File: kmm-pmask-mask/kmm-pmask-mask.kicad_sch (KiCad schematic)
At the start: 68 parts, among them J1 F31L-1A7H1-11030, U1 MS5611-01BA, U10 MAX30101EFD_T, U11 SHT40-AD1B-R3, U12 SHT40-AD1B-R3, U13 TMP117MAIDRVR, U14 TMP117MAIDRVR, U15 TCA9546APW, U2 MAX30101EFD_T, U3 SHT40-AD1B-R3, U4 TMP117MAIDRVR, U5 MS5611-01BA, U6 MS5611-01BA, U7 MS5611-01BA, U8 MAX30101EFD_T, U9 MAX30101EFD_T

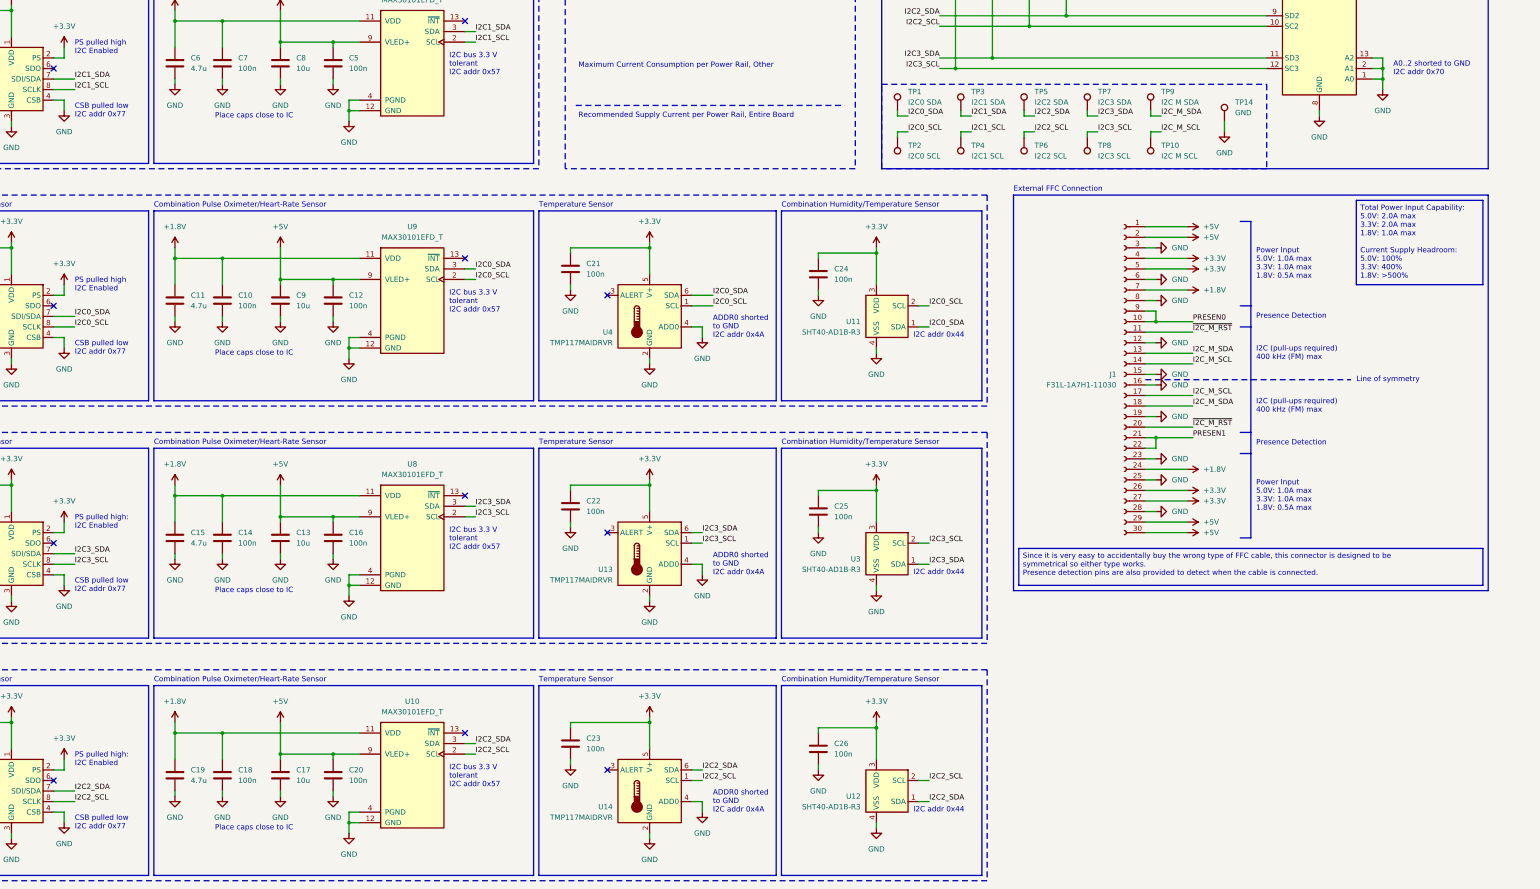
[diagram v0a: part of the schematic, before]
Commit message: Add annotations of bus load
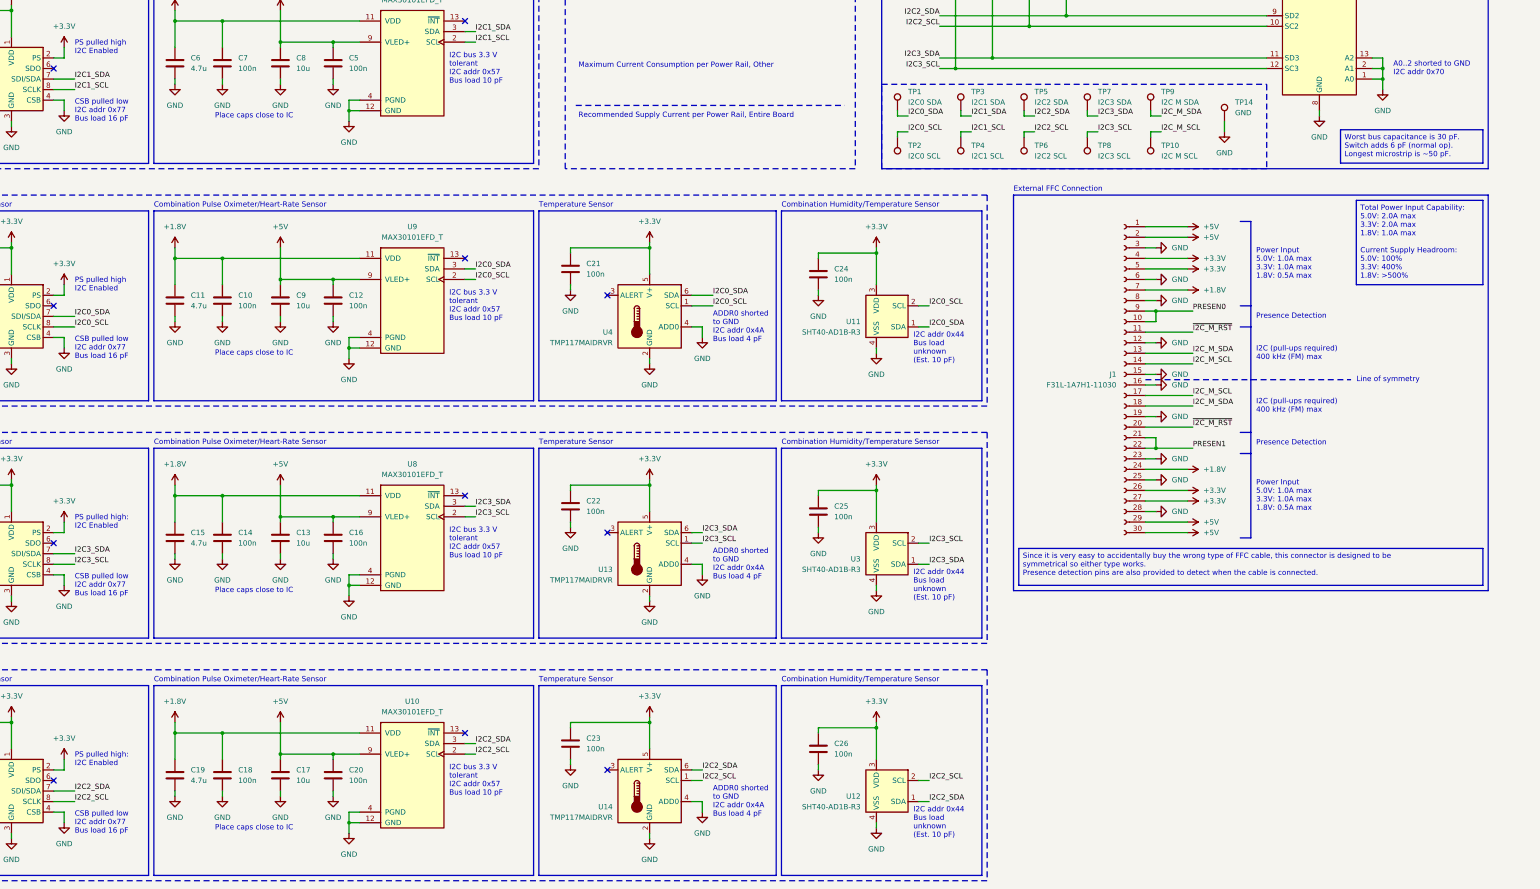
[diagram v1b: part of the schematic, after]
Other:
- note added: "ADDR0 shorted to GND I2C addr 0x4A Bus load 4 pF"
- note added: "CSB pulled low I2C addr 0x77 Bus load 16 pF"
- note added: "I2C addr 0x44 Bus load unknown (Est. 10 pF)"
- note added: "I2C bus 3.3 V tolerant I2C addr 0x57 Bus load 10 pF"
- note removed: "ADDR0 shorted to GND I2C addr 0x4A"
- note removed: "CSB pulled low I2C addr 0x77"
- note removed: "I2C addr 0x44"
- note removed: "I2C bus 3.3 V tolerant I2C addr 0x57"
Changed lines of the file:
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@@
 		)
 	)
-	(text "CSB pulled low\nI2C addr 0x77"
+	(text "CSB pulled low\nI2C addr 0x77\nBus load 16 pF"
 		(exclude_from_sim no)
 		(at 59.69 208.28 0)
@@
 		)
 	)
-	(text "ADDR0 shorted\nto GND\nI2C addr 0x4A"
+	(text "ADDR0 shorted\nto GND\nI2C addr 0x4A\nBus load 4 pF"
 		(exclude_from_sim no)
 		(at 213.36 260.35 0)
@@
 		)
 	)
-	(text "I2C bus 3.3 V\ntolerant\nI2C addr 0x57"
+	(text "I2C bus 3.3 V\ntolerant\nI2C addr 0x57\nBus load 10 pF"
 		(exclude_from_sim no)
 		(at 149.86 80.01 0)
@@
 		)
 	)
-	(text "CSB pulled low\nI2C addr 0x77"
+	(text "CSB pulled low\nI2C addr 0x77\nBus load 16 pF"
 		(exclude_from_sim no)
 		(at 59.69 151.13 0)
@@
 		)
 	)
-	(text "ADDR0 shorted\nto GND\nI2C addr 0x4A"
+	(text "ADDR0 shorted\nto GND\nI2C addr 0x4A\nBus load 4 pF"
 		(exclude_from_sim no)
 		(at 213.36 146.05 0)
@@
 		)
 	)
-	(text "I2C bus 3.3 V\ntolerant\nI2C addr 0x57"
+	(text "I2C bus 3.3 V\ntolerant\nI2C addr 0x57\nBus load 10 pF"
 		(exclude_from_sim no)
 		(at 149.86 194.31 0)
@@
 		)
 	)
-	(text "I2C addr 0x44"
+	(text "I2C addr 0x44\nBus load\nunknown\n(Est. 10 pF)"
 		(exclude_from_sim no)
 		(at 261.62 147.32 0)
@@
 		)
 	)
-	(text "CSB pulled low\nI2C addr 0x77"
+	(text "CSB pulled low\nI2C addr 0x77\nBus load 16 pF"
 		(exclude_from_sim no)
 		(at 59.69 93.98 0)
@@
 		)
 	)
-	(text "ADDR0 shorted\nto GND\nI2C addr 0x4A"
+	(text "ADDR0 shorted\nto GND\nI2C addr 0x4A\nBus load 4 pF"
 		(exclude_from_sim no)
 		(at 213.36 203.2 0)
@@
 		)
 	)
-	(text "I2C bus 3.3 V\ntolerant\nI2C addr 0x57"
+	(text "I2C bus 3.3 V\ntolerant\nI2C addr 0x57\nBus load 10 pF"
 		(exclude_from_sim no)
 		(at 149.86 251.46 0)
@@
 		)
 	)
-	(text "I2C addr 0x44"
+	(text "I2C addr 0x44\nBus load\nunknown\n(Est. 10 pF)"
 		(exclude_from_sim no)
 		(at 261.62 261.62 0)
@@
 		)
 	)
-	(text "I2C bus 3.3 V\ntolerant\nI2C addr 0x57"
+	(text "I2C bus 3.3 V\ntolerant\nI2C addr 0x57\nBus load 10 pF"
 		(exclude_from_sim no)
 		(at 149.86 137.16 0)
@@
 		)
 	)
-	(text "CSB pulled low\nI2C addr 0x77"
+	(text "CSB pulled low\nI2C addr 0x77\nBus load 16 pF"
 		(exclude_from_sim no)
 		(at 59.69 265.43 0)
@@
 		)
 	)
-	(text "I2C addr 0x44"
+	(text "I2C addr 0x44\nBus load\nunknown\n(Est. 10 pF)"
 		(exclude_from_sim no)
 		(at 261.62 204.47 0)
@@
 		)
 	)
+	(text_box "Worst bus capacitance is 30 pF.\nSwitch adds 6 pF (normal op).\nLongest microstrip is ~50 pF."
+		(exclude_from_sim no)
+		(at 364.49 98.5646 0)
+		(size 34.29 8.0376)
+		(margins 0.9525 0.9525 0.9525 0.9525)
+		(stroke
+			(width 0)
+			(type solid)
+		)
+		(fill
+			(type none)
+		)
+		(effects
+			(font
+				(size 1.27 1.27)
+			)
+			(justify left top)
+		)
+	)
 	(junction
 		(at 298.45 71.12)
@@
 	)
 	(junction
-		(at 125.73 265.43)
+		(at 320.04 175.26)
 		(diameter 0)
 		(color 0 0 0 0)
 	)
 	(junction
-		(at 109.22 134.62)
+		(at 125.73 265.43)
 		(diameter 0)
 		(color 0 0 0 0)
 	)
 	(junction
-		(at 95.25 72.39)
+		(at 109.22 134.62)
 		(diameter 0)
 		(color 0 0 0 0)
 	)
 	(junction
-		(at 320.04 144.78)
+		(at 95.25 72.39)
 		(diameter 0)
 		(color 0 0 0 0)
@@
 	)
 	(junction
+		(at 320.04 142.24)
+		(diameter 0)
+		(color 0 0 0 0)
+	)
+	(junction
 		(at 198.12 127)
 		(diameter 0)
@@
 	)
 	(junction
-		(at 320.04 172.72)
-		(diameter 0)
-		(color 0 0 0 0)
-	)
-	(junction
 		(at 83.82 129.54)
 		(diameter 0)
@@
 	(wire
 		(pts
-			(xy 320.04 172.72) (xy 320.04 175.26)
-		)
-		(stroke
-			(width 0)
-			(type default)
-		)
-	)
-	(wire
-		(pts
 			(xy 95.25 243.84) (xy 128.27 243.84)
 		)
@@
 	(wire
 		(pts
-			(xy 320.04 172.72) (xy 328.93 172.72)
+			(xy 320.04 175.26) (xy 328.93 175.26)
 		)
 		(stroke
@@
 	(wire
 		(pts
-			(xy 320.04 144.78) (xy 328.93 144.78)
+			(xy 320.04 142.24) (xy 328.93 142.24)
 		)
 		(stroke
@@
 		)
 	)
+	(wire
+		(pts
+			(xy 320.04 175.26) (xy 320.04 172.72)
+		)
+		(stroke
+			(width 0)
+			(type default)
+		)
+	)
 	(polyline
 		(pts
@@
 	)
 	(label "PRESEN1"
-		(at 328.93 172.72 0)
+		(at 328.93 175.26 0)
 		(effects
 			(font
@@
 	)
 	(label "PRESEN0"
-		(at 328.93 144.78 0)
+		(at 328.93 142.24 0)
 		(effects
 			(font

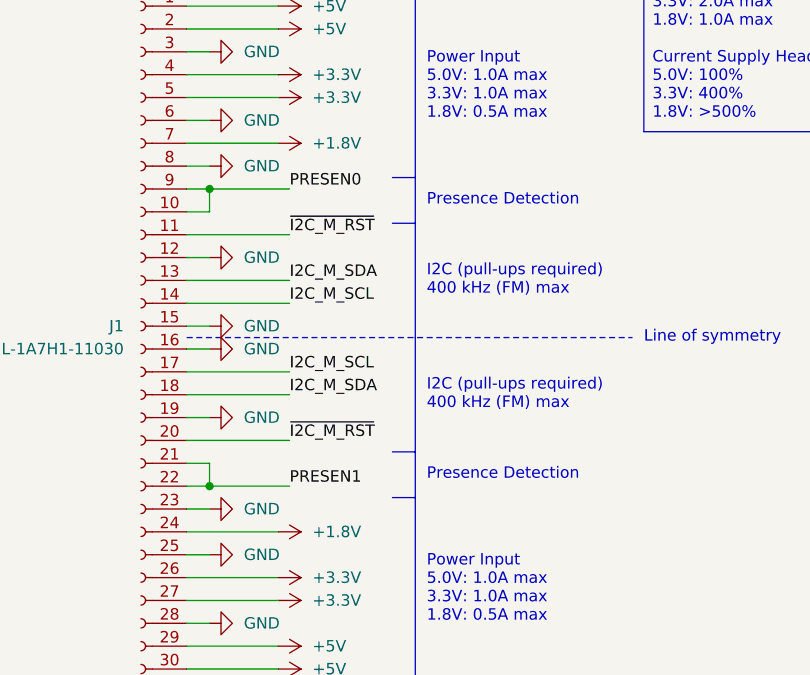
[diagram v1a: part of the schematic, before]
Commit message: tweak FFC cable pinout
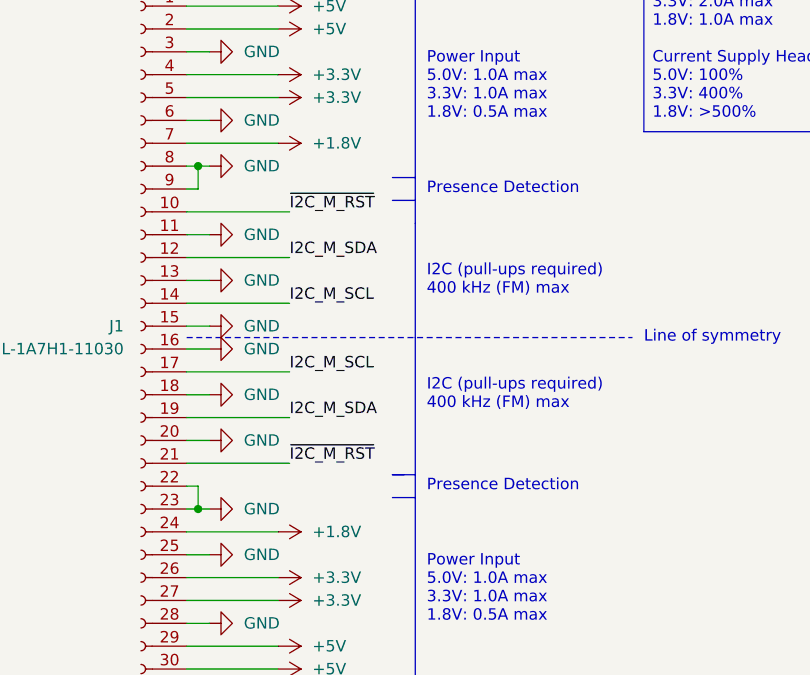
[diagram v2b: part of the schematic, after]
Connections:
- net GND: now also J1.11 (Pin_11), J1.13 (Pin_13), J1.18 (Pin_18), J1.20 (Pin_20), J1.22 (Pin_22), J1.9 (Pin_9); no longer J1.12 (Pin_12), J1.19 (Pin_19)
- net I2C_M_SDA: now also J1.12 (Pin_12), J1.19 (Pin_19); no longer J1.13 (Pin_13), J1.18 (Pin_18)
- net ~{I2C_M_RST}: now also J1.10 (Pin_10), J1.21 (Pin_21); no longer J1.11 (Pin_11), J1.20 (Pin_20)
- removed net PRESEN0: J1.10 (Pin_10), J1.9 (Pin_9)
- removed net PRESEN1: J1.21 (Pin_21), J1.22 (Pin_22)
